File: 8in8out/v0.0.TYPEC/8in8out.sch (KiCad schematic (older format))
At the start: 61 parts, among them IC1 ATTINY48-A, J1 RJ45, J2 RJ45, J3 CONN_6, K110 G5T-1-12VDC, K120 G5T-1-12VDC, K130 G5T-1-12VDC, K140 G5T-1-12VDC, K150 G5T-1-12VDC, K160 G5T-1-12VDC, K170 G5T-1-12VDC, K180 G5T-1-12VDC, P1 CONN_5, P100 CONN_2, P101 CONN_2, P102 CONN_2, P103 CONN_2, P105 CONN_2, P106 CONN_2, P110 CONN_2, P120 CONN_2, P130 CONN_2, P140 CONN_2, P150 CONN_2, P160 CONN_2, P170 CONN_2, P180 CONN_2, P2 CONN_5, P3 CONN_10X2, P4 CONN_2, U1 7805, U10 OPTO-TRANSISTOR, U2 ULN2803, U20 OPTO-TRANSISTOR, U30 OPTO-TRANSISTOR, U40 OPTO-TRANSISTOR, U50 OPTO-TRANSISTOR, U60 OPTO-TRANSISTOR, U70 OPTO-TRANSISTOR, U80 OPTO-TRANSISTOR

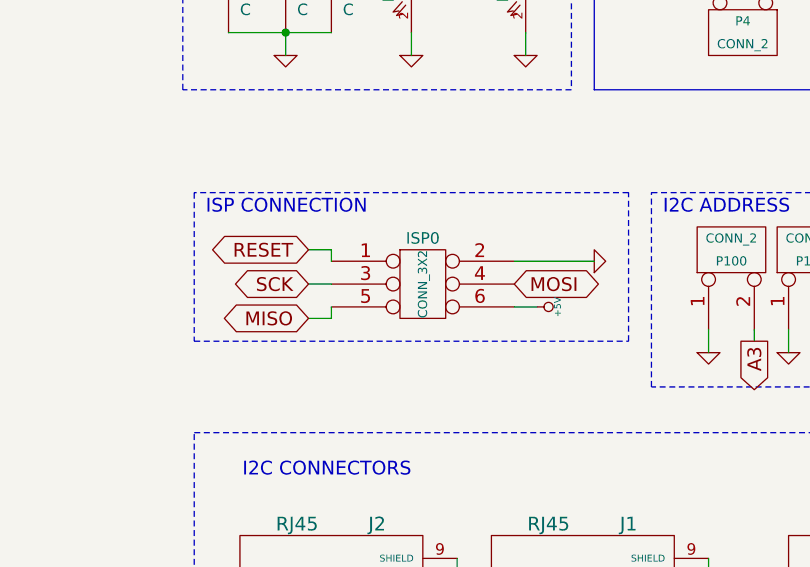
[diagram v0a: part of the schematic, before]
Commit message: correction connecteur ISP
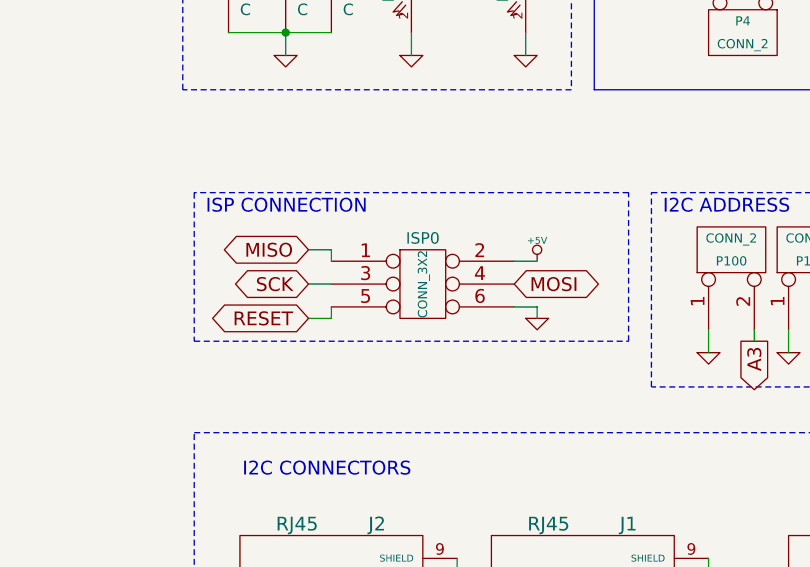
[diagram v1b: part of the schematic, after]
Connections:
- net +5V: now also ISP0.2; no longer ISP0.6
- net GND: now also ISP0.6; no longer ISP0.2
- net MISO: now also ISP0.1; no longer ISP0.5
- net RESET: now also ISP0.5; no longer ISP0.1
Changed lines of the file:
@@
-EESchema Schematic File Version 2  date dim. 02 juin 2013 15:15:57 CEST
+EESchema Schematic File Version 2
 LIBS:g5la-1-12vdc
 LIBS:power
@@
 L +5V #PWR03
 U 1 1 50670686
-P 11800 5050
-F 0 "#PWR03" H 11800 5140 20  0001 C CNN
-F 1 "+5V" H 11800 5140 30  0000 C CNN
-F 2 "" H 11800 5050 60  0001 C CNN
-F 3 "" H 11800 5050 60  0001 C CNN
-	1    11800 5050
-	0    1    1    0
+P 11800 4850
+F 0 "#PWR03" H 11800 4940 20  0001 C CNN
+F 1 "+5V" H 11800 4940 30  0000 C CNN
+F 2 "" H 11800 4850 60  0001 C CNN
+F 3 "" H 11800 4850 60  0001 C CNN
+	1    11800 4850
+	1    0    0    -1
 $EndComp
 Text Notes 10350 4650 0    60   ~ 0
@@
 L GND #PWR025
 U 1 1 5135D759
-P 12050 4850
-F 0 "#PWR025" H 12050 4850 30  0001 C CNN
-F 1 "GND" H 12050 4780 30  0001 C CNN
-F 2 "" H 12050 4850 60  0001 C CNN
-F 3 "" H 12050 4850 60  0001 C CNN
-	1    12050 4850
-	0    -1   -1   0
+P 11800 5100
+F 0 "#PWR025" H 11800 5100 30  0001 C CNN
+F 1 "GND" H 11800 5030 30  0001 C CNN
+F 2 "" H 11800 5100 60  0001 C CNN
+F 3 "" H 11800 5100 60  0001 C CNN
+	1    11800 5100
+	1    0    0    -1
 $EndComp
 $Comp
@@
 RESET
 Connection ~ 13700 10550
-Text GLabel 10800 4800 0    60   BiDi ~ 0
+Text GLabel 10800 5100 0    60   BiDi ~ 0
 RESET
 Text GLabel 10800 4950 0    60   BiDi ~ 0
 SCK
-Text GLabel 10800 5100 0    60   BiDi ~ 0
+Text GLabel 10800 4800 0    60   BiDi ~ 0
 MISO
 Text GLabel 11700 4950 2    60   BiDi ~ 0
@@
 Wire Wire Line
 	10900 5100 10900 5050
-Wire Wire Line
-	11700 4850 12050 4850
 $Comp
 L CONN_5 P1
@@
 Connection ~ 10450 3400
 Connection ~ 10900 3400
+Wire Wire Line
+	11800 5050 11800 5100
+Wire Wire Line
+	11700 4850 11800 4850
 $EndSCHEMATC
